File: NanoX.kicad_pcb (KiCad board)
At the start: 2 copper layers, 73.9 x 18.1 mm, 47 parts, among them J1 10118192-0001LF, J2 Conn_ARM_JTAG_SWD_10, J3 Conn_01x11, J4 NanoClassic_R, J5 Conn_01x11, J6 NanoClassic_L, SW1 SW_Push, U1 ATSAMD21G18A-AUT, U2 MCP1725-1202E_SN, U3 CAT24C16YI-GT3

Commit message: Add Github link, remove bak file.
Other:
- board text added: "NanoX Rev. P1 https://github.com/Bu-Gee/NanoX Copyright(c) 2020, Fortian Inc. Licensed Under CC-BY-NC-SA 3.0"
- board text removed: "NanoX Rev. P1 Copyright(c) 2020, Fortian Inc. Licensed Under CC-BY-NC-SA 3.0"
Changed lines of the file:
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@@
     (effects (font (size 0.8 0.8) (thickness 0.15)))
   )
-  (gr_text "NanoX   Rev. P1\nCopyright(c) 2020, Fortian Inc.\nLicensed Under CC-BY-NC-SA 3.0\n" (at 136.398 91.694) (layer B.SilkS)
+  (gr_text "NanoX   Rev. P1\nhttps://github.com/Bu-Gee/NanoX\nCopyright(c) 2020, Fortian Inc.\nLicensed Under CC-BY-NC-SA 3.0\n" (at 136.398 91.694) (layer B.SilkS)
     (effects (font (size 0.8 0.8) (thickness 0.15)) (justify mirror))
   )

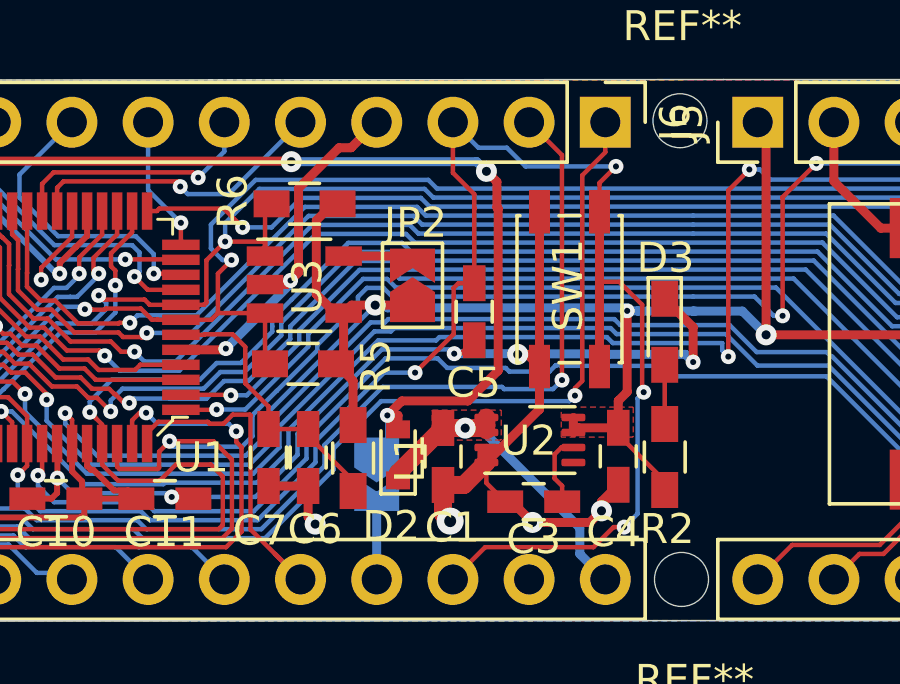
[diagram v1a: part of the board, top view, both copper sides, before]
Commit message: Rework pads, add Digikey part numbers.
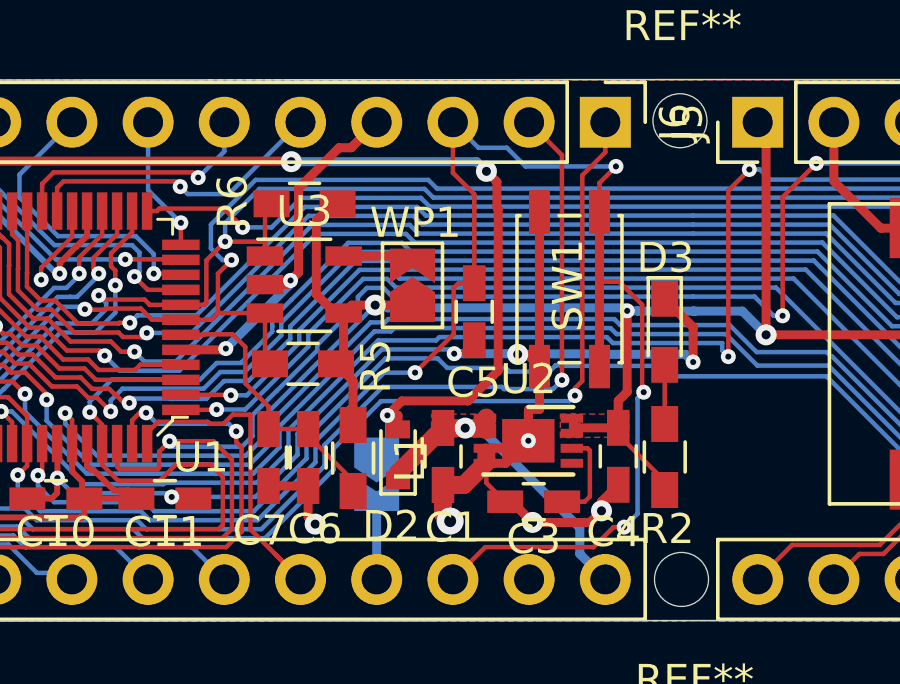
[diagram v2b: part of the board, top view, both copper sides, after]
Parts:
- U2: value MCP1725-1202E_SN -> MCP1725-3302E_MC; footprint Package_DFN_QFN:DFN-8-3x2mm_P0.5mm -> Package_DFN_QFN:DFN-8-1EP_3x2mm_P0.5mm_EP1.75x1.45mm
- renumbered VUSB to VUSB1, JP2 to WP1
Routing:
- net GND: track 105.9 -> 108.6 mm, vias 23 -> 24
- net Net-(C3-Pad1): track 2.40 -> 3.16 mm
